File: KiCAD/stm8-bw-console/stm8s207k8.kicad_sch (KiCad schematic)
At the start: 27 parts, among them J1 SWIM con., J2 video out, SW1 power, SW2 LEFT, SW3 UP, SW4 DOWN, SW5 RIGHT, SW6 B, SW7 A, U1 STM8S103F3M, Y1 16Mhz

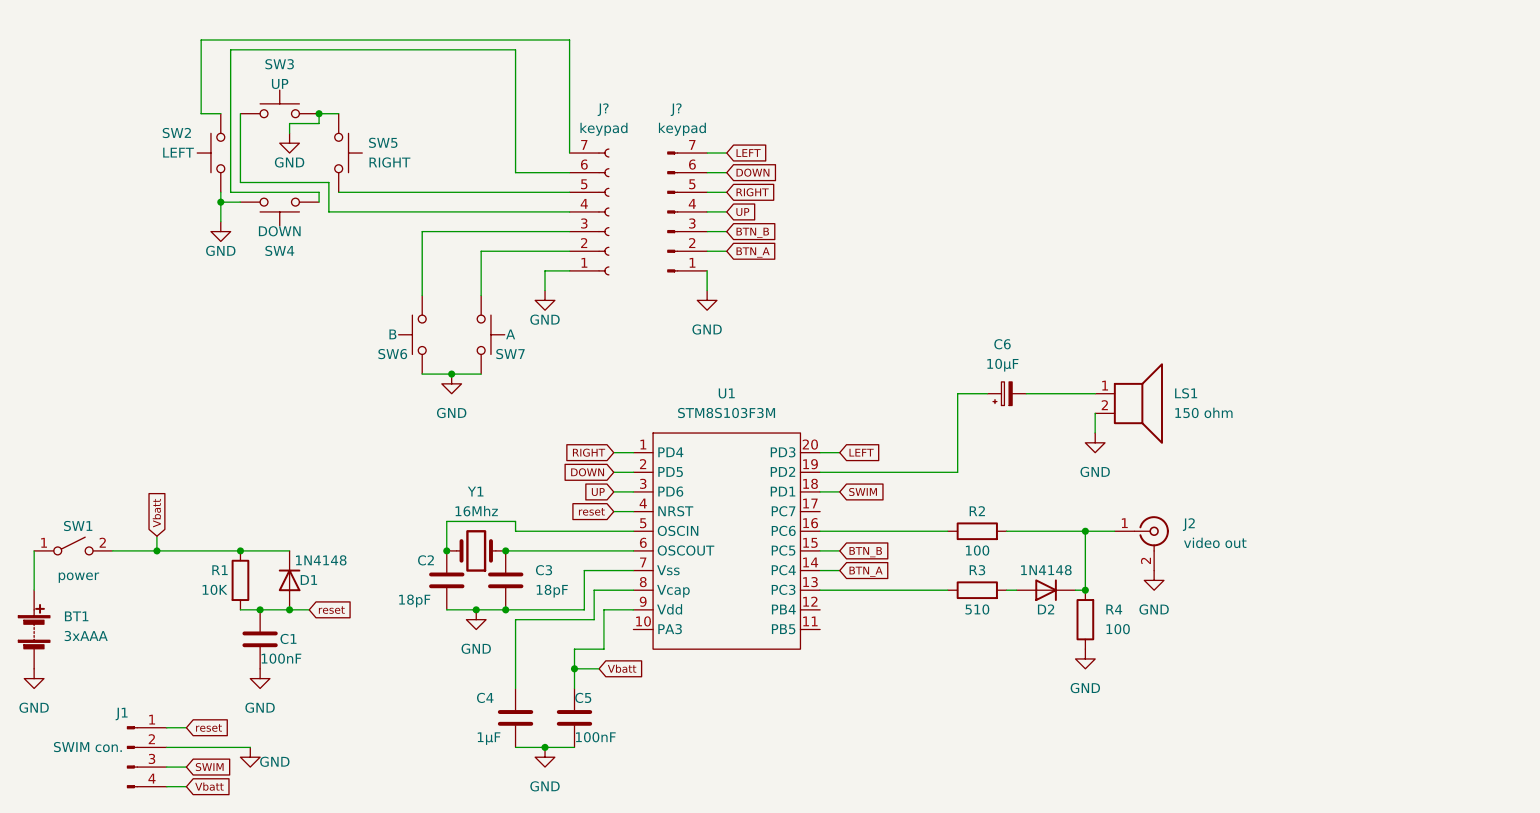
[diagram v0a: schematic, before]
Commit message: assemblage nouveau circuit et tests préléminaires
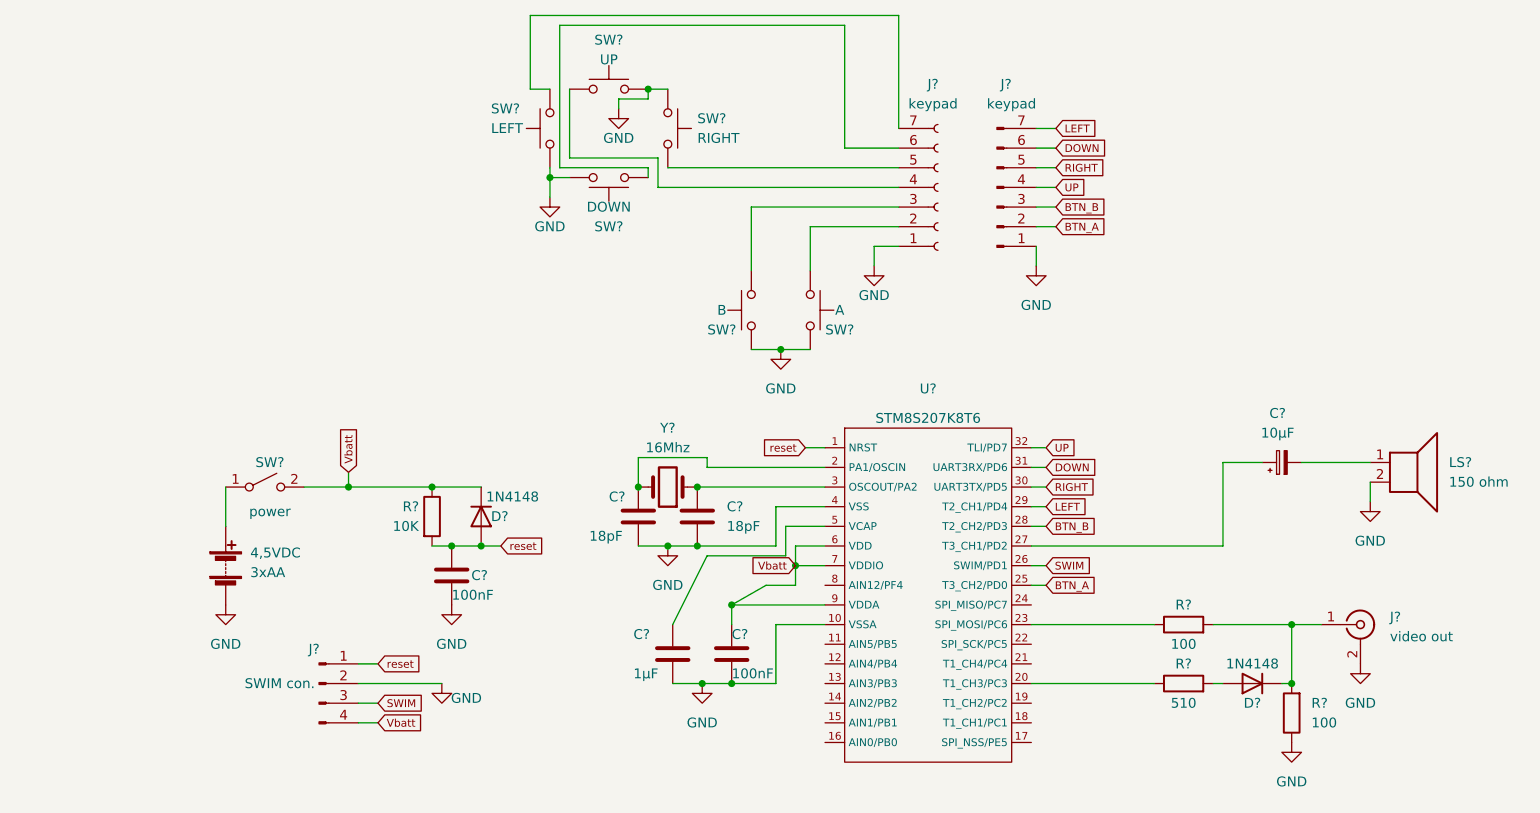
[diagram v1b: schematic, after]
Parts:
- removed BT1: 3xAAA, symbol Device:Battery
- removed C1, C5: 100nF, symbol Device:C
- removed C2, C3: 18pF, symbol Device:C
- removed C4: 1µF, symbol Device:C
- removed C6: 10µF, symbol Device:C_Polarized_Small
- removed D1, D2: 1N4148, Diode_THT:D_DO-35_SOD27_P7.62mm_Horizontal, symbol Diode:1N4148
- removed J1: SWIM con., symbol Connector:Conn_01x04_Male
- removed J2: video out, symbol Connector:Conn_Coaxial
- removed J?: keypad, symbol Connector:Conn_01x07_Male
- removed J?: keypad, symbol Connector:Conn_01x07_Female
- removed LS1: 150 ohm, symbol Device:Speaker
- removed R1: 10K, symbol Device:R
- removed R2, R4: 100, symbol Device:R
- removed R3: 510, symbol Device:R
- removed SW1: power, symbol Switch:SW_SPST
- removed SW2: LEFT, symbol Switch:SW_MEC_5G
- removed SW3: UP, symbol Switch:SW_MEC_5G
- removed SW4: DOWN, symbol Switch:SW_MEC_5G
- removed SW5: RIGHT, symbol Switch:SW_MEC_5G
- removed SW6: B, symbol Switch:SW_MEC_5G
- removed SW7: A, symbol Switch:SW_MEC_5G
- removed U1: STM8S103F3M, symbol MCU_ST_STM8:STM8S103F3M
- removed Y1: 16Mhz, symbol Device:Crystal
- added 4,5VDC: 3xAA, symbol Device:Battery
- added C? (x2): 18pF, symbol Device:C
- added C?: 10µF, symbol Device:C_Polarized_Small
- added C?: 1µF, symbol Device:C
- added C? (x2): 100nF, symbol Device:C
- added D? (x2): 1N4148, Diode_THT:D_DO-35_SOD27_P7.62mm_Horizontal, symbol Diode:1N4148
- added J?: video out, symbol Connector:Conn_Coaxial
- added J?: keypad, symbol Connector:Conn_01x07_Male
- added J?: keypad, symbol Connector:Conn_01x07_Female
- added J?: SWIM con., symbol Connector:Conn_01x04_Male
- added LS?: 150 ohm, symbol Device:Speaker
- added R?: 510, symbol Device:R
- added R?: 10K, symbol Device:R
- added R? (x2): 100, symbol Device:R
- added SW?: UP, symbol Switch:SW_MEC_5G
- added SW?: LEFT, symbol Switch:SW_MEC_5G
- added SW?: A, symbol Switch:SW_MEC_5G
- added SW?: B, symbol Switch:SW_MEC_5G
- added SW?: RIGHT, symbol Switch:SW_MEC_5G
- added SW?: power, symbol Switch:SW_SPST
- added SW?: DOWN, symbol Switch:SW_MEC_5G
- added U?: STM8S207K8T6, symbol MCU_ST_STM8:STM8S207K8T6
- added Y?: 16Mhz, symbol Device:Crystal
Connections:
- net BTN_A: now also J?.2 (Pin_2), U?.25 (T3_CH2/PD0)
- net BTN_B: now also J?.3 (Pin_3), U?.28 (T2_CH2/PD3)
- net DOWN: now also J?.6 (Pin_6), U?.31 (UART3RX/PD6)
- net GND: now also 4,5VDC.2 (-), C?.2, C?.2, C?.2, C?.2, C?.2, J?.1 (Pin_1), J?.1 (Pin_1), J?.2 (Ext), J?.2 (Pin_2), LS?.2, R?.1, SW?.1 (A), SW?.1 (A), SW?.1 (A), SW?.2 (A), SW?.2 (A), SW?.2 (A), SW?.3 (B), SW?.3 (B), SW?.3 (B), SW?.4 (B), SW?.4 (B), SW?.4 (B), U?.10 (VSSA), U?.4 (VSS)
- net LEFT: now also J?.7 (Pin_7), U?.29 (T2_CH1/PD4)
- net RIGHT: now also J?.5 (Pin_5), U?.30 (UART3TX/PD5)
- net SWIM: now also J?.3 (Pin_3), U?.26 (SWIM/PD1)
- net UP: now also J?.4 (Pin_4), U?.32 (TLI/PD7)
- net Vbatt: now also C?.1, D?.1 (K), J?.4 (Pin_4), R?.1, SW?.2 (B), U?.6 (VDD), U?.7 (VDDIO), U?.9 (VDDA)
- net reset: now also C?.1, D?.2 (A), J?.1 (Pin_1), R?.2, U?.1 (NRST)
- new net: R?.1, U?.20 (T1_CH3/PC3)
- new net: D?.2 (A), R?.2
- new net: D?.1 (K), J?.1 (In), R?.2, R?.2
- new net: J?.4 (Pin_4), SW?.1 (A), SW?.2 (A)
- new net: C?.1, U?.2 (PA1/OSCIN), Y?.2
- new net: C?.1, U?.27 (T3_CH1/PD2)
- new net: C?.2, LS?.1
- new net: C?.1, U?.5 (VCAP)
- new net: C?.1, U?.3 (OSCOUT/PA2), Y?.1
- new net: R?.1, U?.23 (SPI_MOSI/PC6)
- new net: J?.2 (Pin_2), SW?.1 (A), SW?.2 (A)
- new net: J?.3 (Pin_3), SW?.3 (B), SW?.4 (B)
- new net: J?.5 (Pin_5), SW?.3 (B), SW?.4 (B)
- new net: J?.6 (Pin_6), SW?.1 (A), SW?.2 (A)
- new net: J?.7 (Pin_7), SW?.3 (B), SW?.4 (B)
- new net: 4,5VDC.1 (+), SW?.1 (A)
